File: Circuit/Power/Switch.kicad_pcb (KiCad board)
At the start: 2 copper layers, 92.7 x 30.5 mm, 40 parts, among them J1 Main Power In, J2 To Starter, J3 To Capacitor, J4 To Injector, J5 To Coil, J6 To Control Power, J7 From Control, J8 To Coil Signal, Q1 RFP30N06LE, Q2 RFP30N06LE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

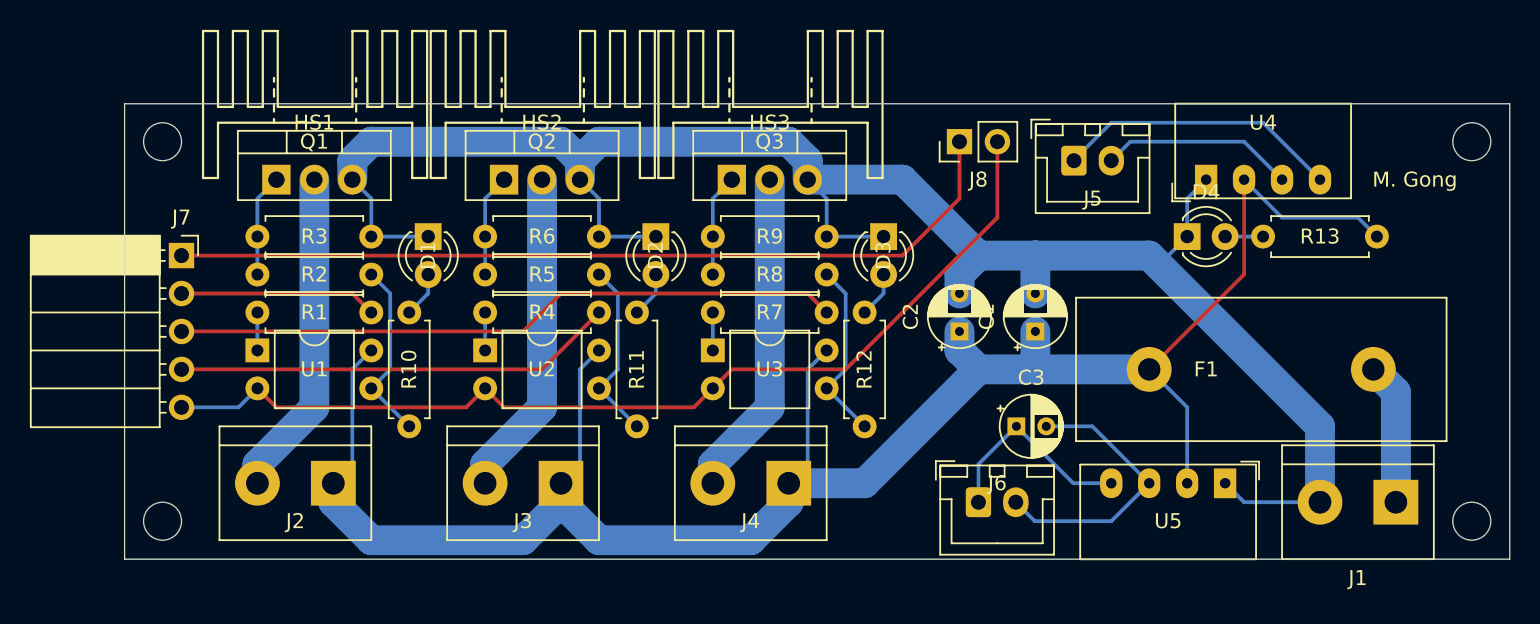
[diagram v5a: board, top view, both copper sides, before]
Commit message: [Circuit] Adjust the resistors to adapt to 5V control power
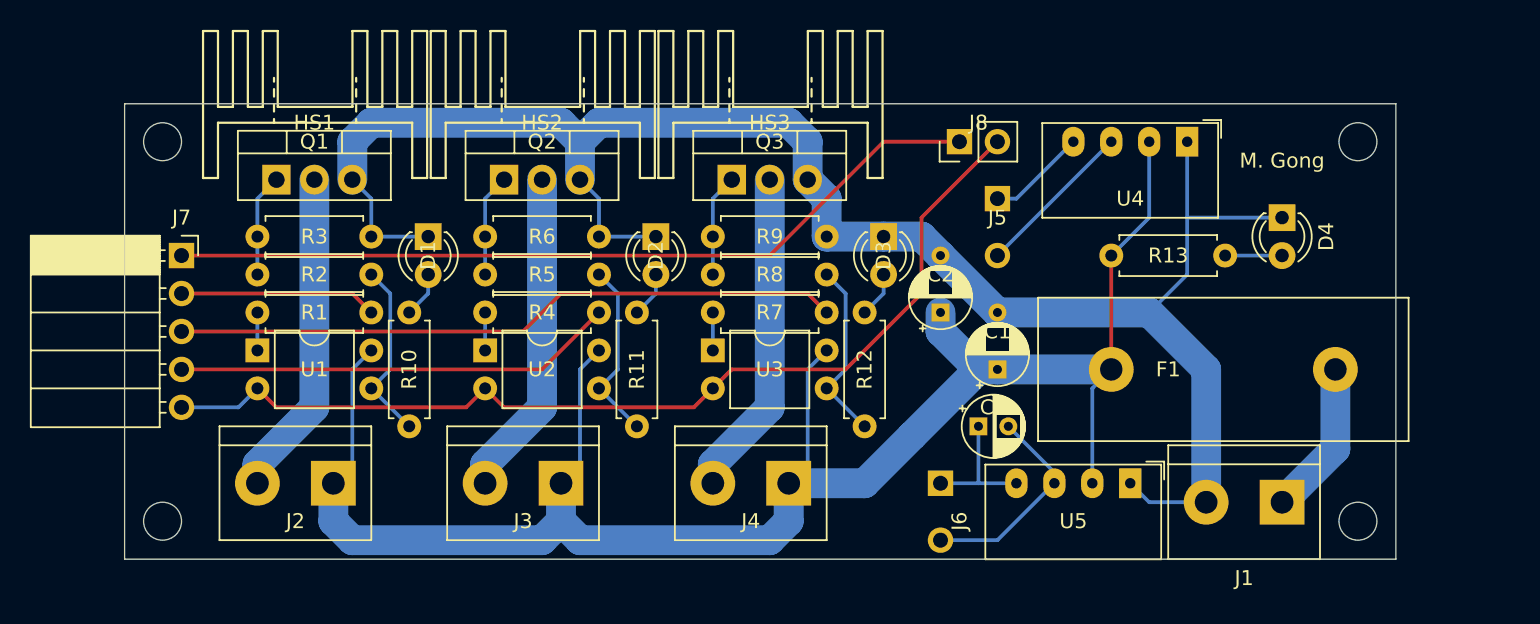
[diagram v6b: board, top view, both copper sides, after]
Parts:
- J5, J6: footprint Connector_JST:JST_XH_B2B-XH-A_1x02_P2.50mm_Vertical -> Connector_Wire:SolderWirePad_1x02_P3.81mm_Drill1mm
- R1, R4, R7: value 1K -> 680
- moved R13 17.8 mm to (141.0, 80.0), turned to 0 degrees
- moved J1 7.62 mm to (152.4, 96.5)
- moved D4 6.48 mm to (152.4, 77.5), turned to 270 degrees
- moved U5 6.35 mm to (142.2, 95.2)
- moved J5 5.72 mm to (133.3, 76.2), turned to 270 degrees
- moved C1 3.59 mm to (133.3, 87.6)
- moved J6 2.84 mm to (129.5, 95.2), turned to 270 degrees
- moved U4 2.84 mm to (146.1, 72.4), turned to 270 degrees
- moved C3 2.54 mm to (132.1, 91.4)
- moved F1 2.54 mm to (141.0, 87.6)
- moved C2 1.80 mm to (129.5, 83.8)
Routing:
- net /CoilPower+: track 19.1 -> 6.66 mm
- net /CapacitorPower+: track 135.7 -> 124.1 mm
- net /ControlPower+: track 14.1 -> 8.89 mm
- net /ControlPower-: track 19.0 -> 14.3 mm
- net /PowerIn-: track 126.6 -> 123.2 mm
- net /CoilSignal: track 57.5 -> 55.2 mm
- net /CoilPower-: track 13.0 -> 10.8 mm
- net Net-(D4-Pad2): track 2.54 -> 3.81 mm
- net /PowerIn+: track 9.52 -> 10.4 mm
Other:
- board size 92.7 x 30.5 mm -> 85.1 x 30.5 mm

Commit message: [Circuit] Adjust the gate resistors
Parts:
- R2, R5, R8: value 10K -> 4.7K
- moved J6 3.59 mm to (127.0, 97.8), turned to 0 degrees
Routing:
- net /ControlPower+: track 8.89 -> 12.0 mm
- net /ControlPower-: track 14.3 -> 12.5 mm
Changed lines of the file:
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@@
   )
   (module Connector_Wire:SolderWirePad_1x02_P3.81mm_Drill1mm (layer F.Cu)
-    (at 129.54 95.25 270)
+    (at 127 97.79)
     (descr "Wire solder connection")
     (tags connector)
     (attr virtual)
-    (fp_text reference J6 (at 2.54 -1.27 270) (layer F.SilkS)
-      (effects (font (size 1 1) (thickness 0.15)))
-    )
-    (fp_text value "To Control Power" (at 2.54 1.27 90) (layer F.Fab)
-      (effects (font (size 1 1) (thickness 0.15)))
-    )
-    (fp_text user %R (at 2.54 -1.27 90) (layer F.Fab)
+    (fp_text reference J6 (at 2.54 -1.27 180) (layer F.SilkS)
+      (effects (font (size 1 1) (thickness 0.15)))
+    )
+    (fp_text value "To Control Power" (at 2.54 1.27) (layer F.Fab)
+      (effects (font (size 1 1) (thickness 0.15)))
+    )
+    (fp_text user %R (at 2.54 -1.27) (layer F.Fab)
       (effects (font (size 1 1) (thickness 0.15)))
     )
@@
     (fp_line (start 5.56 1.75) (end 5.56 -1.75) (layer F.CrtYd) (width 0.05))
     (fp_line (start 5.56 1.75) (end -1.74 1.75) (layer F.CrtYd) (width 0.05))
-    (pad 1 thru_hole rect (at 0 0 270) (size 1.7 1.7) (drill 1) (layers *.Cu *.Mask)
+    (pad 1 thru_hole rect (at 0 0) (size 1.7 1.7) (drill 1) (layers *.Cu *.Mask)
       (net 24 /ControlPower+))
-    (pad 2 thru_hole circle (at 3.81 0 270) (size 1.7 1.7) (drill 1) (layers *.Cu *.Mask)
+    (pad 2 thru_hole circle (at 3.81 0) (size 1.7 1.7) (drill 1) (layers *.Cu *.Mask)
       (net 23 /ControlPower-))
   )
@@
       (effects (font (size 1 1) (thickness 0.15)))
     )
-    (fp_text value 10K (at 2.54 0) (layer F.Fab)
+    (fp_text value 4.7K (at 2.54 0) (layer F.Fab)
       (effects (font (size 1 1) (thickness 0.15)))
     )
@@
       (effects (font (size 1 1) (thickness 0.15)))
     )
-    (fp_text value 10K (at 2.54 0) (layer F.Fab)
+    (fp_text value 4.7K (at 2.54 0) (layer F.Fab)
       (effects (font (size 1 1) (thickness 0.15)))
     )
@@
       (effects (font (size 1 1) (thickness 0.15)))
     )
-    (fp_text value 10K (at 2.54 0) (layer F.Fab)
+    (fp_text value 4.7K (at 2.54 0) (layer F.Fab)
       (effects (font (size 1 1) (thickness 0.15)))
     )
@@
   (segment (start 146.05 72.39) (end 146.05 77.47) (width 0.25) (layer B.Cu) (net 22) (status 10))
   (segment (start 146.05 77.47) (end 146.05 81.28) (width 0.25) (layer B.Cu) (net 22))
-  (segment (start 137.16 95.25) (end 133.35 99.06) (width 0.25) (layer B.Cu) (net 23) (status 10))
-  (segment (start 129.54 99.06) (end 133.35 99.06) (width 0.25) (layer B.Cu) (net 23) (status 10))
   (segment (start 137.16 94.52) (end 134.08 91.44) (width 0.25) (layer B.Cu) (net 23))
   (segment (start 137.16 95.25) (end 137.16 94.52) (width 0.25) (layer B.Cu) (net 23))
-  (segment (start 132.08 91.44) (end 132.08 95.25) (width 0.25) (layer B.Cu) (net 24))
-  (segment (start 134.62 95.25) (end 132.08 95.25) (width 0.25) (layer B.Cu) (net 24))
-  (segment (start 132.08 95.25) (end 129.54 95.25) (width 0.25) (layer B.Cu) (net 24))
+  (segment (start 137.16 95.25) (end 134.62 97.79) (width 0.25) (layer B.Cu) (net 23))
+  (segment (start 134.62 97.79) (end 130.81 97.79) (width 0.25) (layer B.Cu) (net 23))
+  (segment (start 134.62 95.25) (end 132.08 92.71) (width 0.25) (layer B.Cu) (net 24))
+  (segment (start 132.08 92.71) (end 132.08 91.44) (width 0.25) (layer B.Cu) (net 24))
+  (segment (start 132.08 92.71) (end 127 97.79) (width 0.25) (layer B.Cu) (net 24))
   (segment (start 155.97 92.95) (end 152.4 96.52) (width 2) (layer B.Cu) (net 25) (status 20))
   (segment (start 155.97 92.95) (end 155.97 87.63) (width 2) (layer B.Cu) (net 25) (status 20))

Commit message: [Circuit] Upgrade to KiCad 6 format
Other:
- net class Default removed
